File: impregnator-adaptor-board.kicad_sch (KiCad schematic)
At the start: 20 parts, among them J1 1932588, J10 1935336, J11 Conn_01x16_Socket, J12 Conn_01x16_Socket, J13 Conn_01x24_Socket, J14 Conn_01x24_Socket, J15 1935336, J16 1935336, J2 Conn_01x16_Socket, J3 Conn_01x16_Socket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

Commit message: project native components
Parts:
- J1: footprint 1932588:PHOENIX_1932588 -> impregnator-adaptor-board:PHOENIX_1932588; symbol 1932588:1932588 -> impregnator-adaptor-board:1932588
- J10, J15, J16, J8, J9: footprint 1935336:PHOENIX_1935336 -> impregnator-adaptor-board:PHOENIX_1935336; symbol 1935336:1935336 -> impregnator-adaptor-board:1935336
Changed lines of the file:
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@@
 	)
 	(symbol
-		(lib_id "1935336:1935336")
+		(lib_id "impregnator-adaptor-board:1935336")
 		(at 229.87 130.81 0)
 		(unit 1)
@@
 			)
 		)
-		(property "Footprint" "1935336:PHOENIX_1935336"
+		(property "Footprint" "impregnator-adaptor-board:PHOENIX_1935336"
 			(at 229.87 130.81 0)
 			(effects
@@
 	)
 	(symbol
-		(lib_id "1935336:1935336")
+		(lib_id "impregnator-adaptor-board:1935336")
 		(at 196.85 130.81 0)
 		(unit 1)
@@
 			)
 		)
-		(property "Footprint" "1935336:PHOENIX_1935336"
+		(property "Footprint" "impregnator-adaptor-board:PHOENIX_1935336"
 			(at 196.85 130.81 0)
 			(effects
@@
 	)
 	(symbol
-		(lib_id "1935336:1935336")
+		(lib_id "impregnator-adaptor-board:1935336")
 		(at 215.9 153.67 0)
 		(unit 1)
@@
 			)
 		)
-		(property "Footprint" "1935336:PHOENIX_1935336"
+		(property "Footprint" "impregnator-adaptor-board:PHOENIX_1935336"
 			(at 215.9 153.67 0)
 			(effects
@@
 	)
 	(symbol
-		(lib_id "1932588:1932588")
+		(lib_id "impregnator-adaptor-board:1932588")
 		(at 143.51 19.05 90)
 		(unit 1)
@@
 			)
 		)
-		(property "Footprint" "1932588:PHOENIX_1932588"
+		(property "Footprint" "impregnator-adaptor-board:PHOENIX_1932588"
 			(at 143.51 19.05 0)
 			(effects
@@
 	)
 	(symbol
-		(lib_id "1935336:1935336")
+		(lib_id "impregnator-adaptor-board:1935336")
 		(at 262.89 130.81 0)
 		(unit 1)
@@
 			)
 		)
-		(property "Footprint" "1935336:PHOENIX_1935336"
+		(property "Footprint" "impregnator-adaptor-board:PHOENIX_1935336"
 			(at 262.89 130.81 0)
 			(effects
@@
 	)
 	(symbol
-		(lib_id "1935336:1935336")
+		(lib_id "impregnator-adaptor-board:1935336")
 		(at 250.19 153.67 0)
 		(unit 1)
@@
 			)
 		)
-		(property "Footprint" "1935336:PHOENIX_1935336"
+		(property "Footprint" "impregnator-adaptor-board:PHOENIX_1935336"
 			(at 250.19 153.67 0)
 			(effects

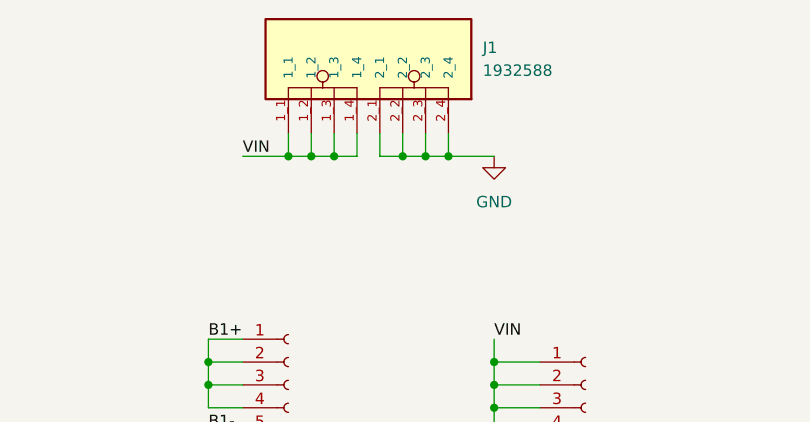
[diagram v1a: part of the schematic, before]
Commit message: use smaller central screw connector
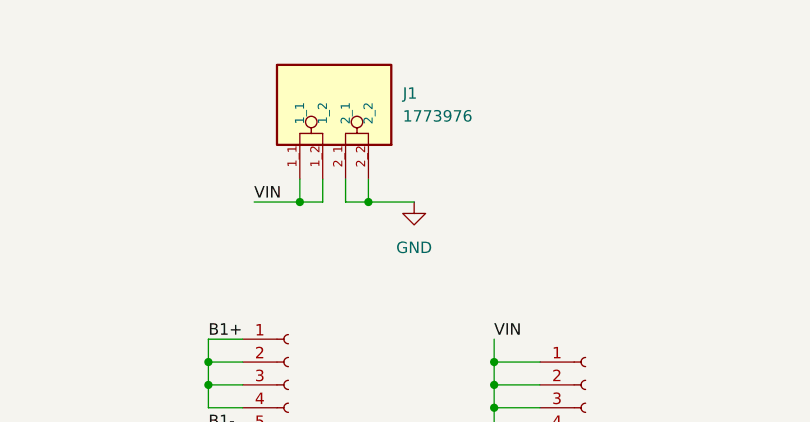
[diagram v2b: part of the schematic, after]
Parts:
- removed J1: 1932588, impregnator-adaptor-board:PHOENIX_1932588, symbol impregnator-adaptor-board:1932588
- added J1: 1773976, impregnator-adaptor-board:PHOENIX_1773976, symbol impregnator-adaptor-board:1773976
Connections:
- net GND: now also J1.2_1, J1.2_2
- net VIN: now also J1.1_1, J1.1_2

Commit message: put all slots on the same side and add silkscreen
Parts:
- added H5: MountingHole_Pad, MountingHole:MountingHole_3.2mm_M3_DIN965_Pad, symbol Mechanical:MountingHole_Pad
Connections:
- no-connect marks 3 -> 4
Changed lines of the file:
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@@
 		(at 240.03 41.91)
 	)
+	(no_connect
+		(at 240.03 78.74)
+	)
 	(wire
 		(pts
@@
 					(unit 1)
 				)
+			)
+		)
+	)
+	(symbol
+		(lib_id "Mechanical:MountingHole_Pad")
+		(at 240.03 76.2 0)
+		(unit 1)
+		(exclude_from_sim yes)
+		(in_bom no)
+		(on_board yes)
+		(dnp no)
+		(fields_autoplaced yes)
+		(property "Reference" "H5"
+			(at 242.57 73.6599 0)
+			(effects
+				(font
+					(size 1.27 1.27)
+				)
+				(justify left)
+			)
+		)
+		(property "Value" "MountingHole_Pad"
+			(at 242.57 76.1999 0)
+			(effects
+				(font
+					(size 1.27 1.27)
+				)
+				(justify left)
+			)
+		)
+		(property "Footprint" "MountingHole:MountingHole_3.2mm_M3_DIN965_Pad"
+			(at 240.03 76.2 0)
+			(effects
+				(font
+					(size 1.27 1.27)
+				)
+				(hide yes)
+			)
+		)
+		(property "Datasheet" "~"
+			(at 240.03 76.2 0)
+			(effects
+				(font
+					(size 1.27 1.27)
+				)
+				(hide yes)
+			)
+		)
+		(property "Description" "Mounting Hole with connection"
+			(at 240.03 76.2 0)
+			(effects
+				(font
+					(size 1.27 1.27)
+				)
+				(hide yes)
+			)
+		)
+		(pin "1"
+		)
+		(instances
+			(project "impregnator-adaptor-board"
+				(path "/2515d7cc-c78a-4059-b5ba-d6a4dc125d5f"
+					(reference "H5")
+					(unit 1)
+				)
